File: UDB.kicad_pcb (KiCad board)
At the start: 4 copper layers, 18 x 16.5 mm, 13 parts, among them J1 TYPE-C-31-M12_13, J2 X1224WRS-04-LPV01, U1 TPD4E05U06DQAR

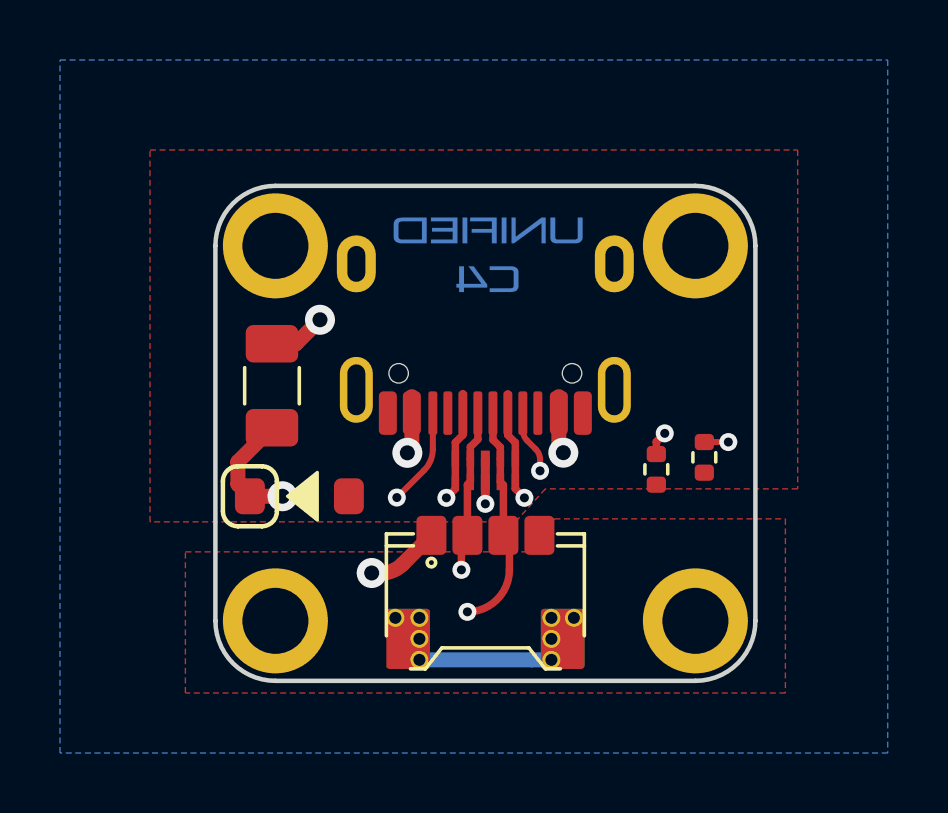
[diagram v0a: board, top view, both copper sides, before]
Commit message: Add C5 logo and -EZM marking; update prod files
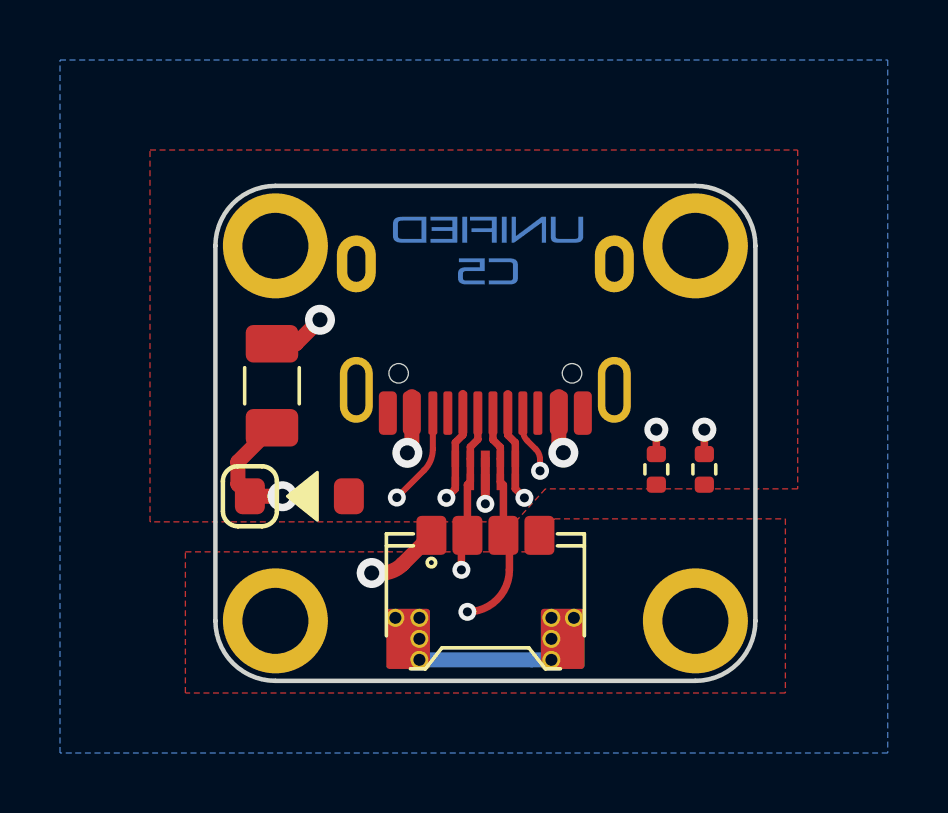
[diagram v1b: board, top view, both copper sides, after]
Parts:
- moved R2 0.40 mm to (82.3, 66.0)
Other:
- board text added: "5.1k"
- board text added: "V5.0-EZM"
- board text removed: "V5.0"
